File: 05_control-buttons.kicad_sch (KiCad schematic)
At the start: 8 parts, among them SW1 SW_Push, SW2 SW_Push, SW3 SW_Push, SW4 SW_Push

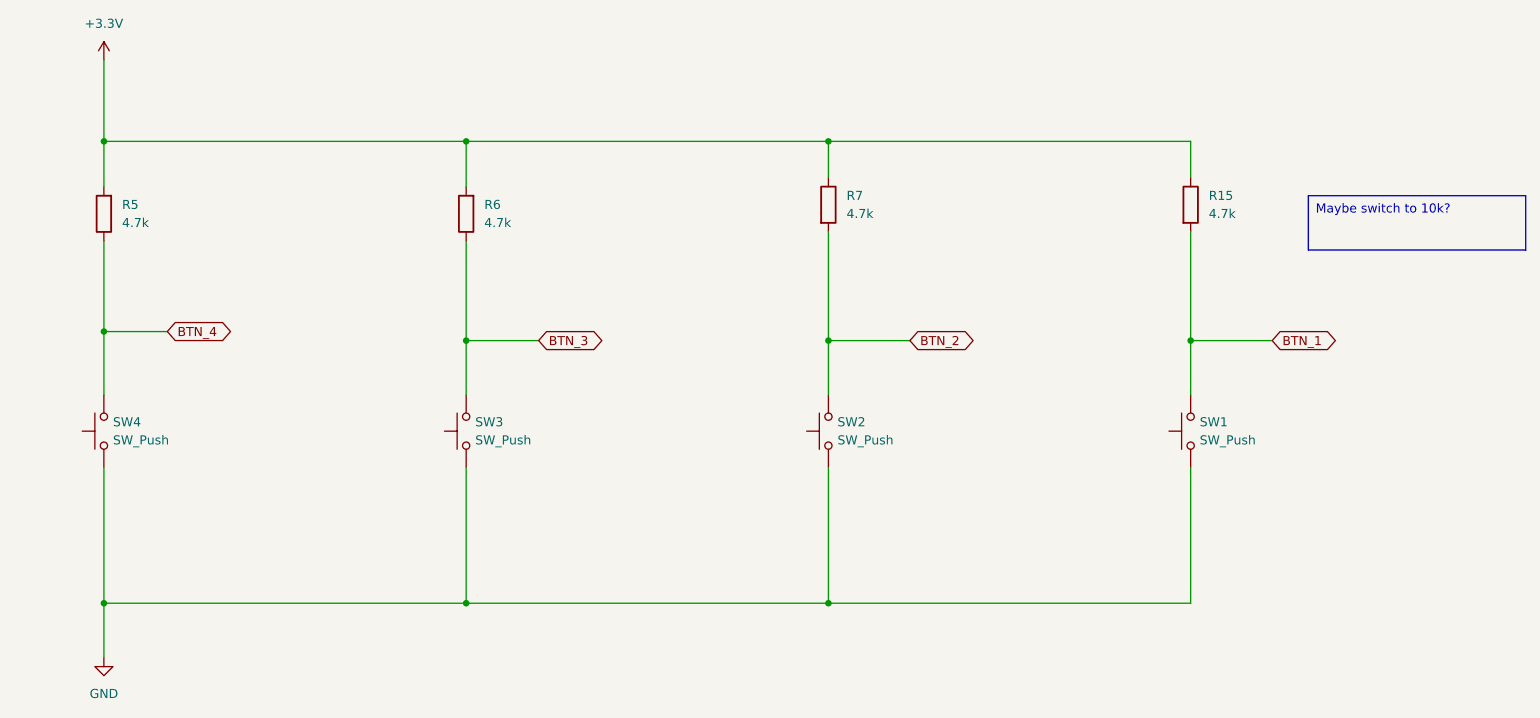
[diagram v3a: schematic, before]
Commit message: Migrate to KiCad 9, start working on the new revision
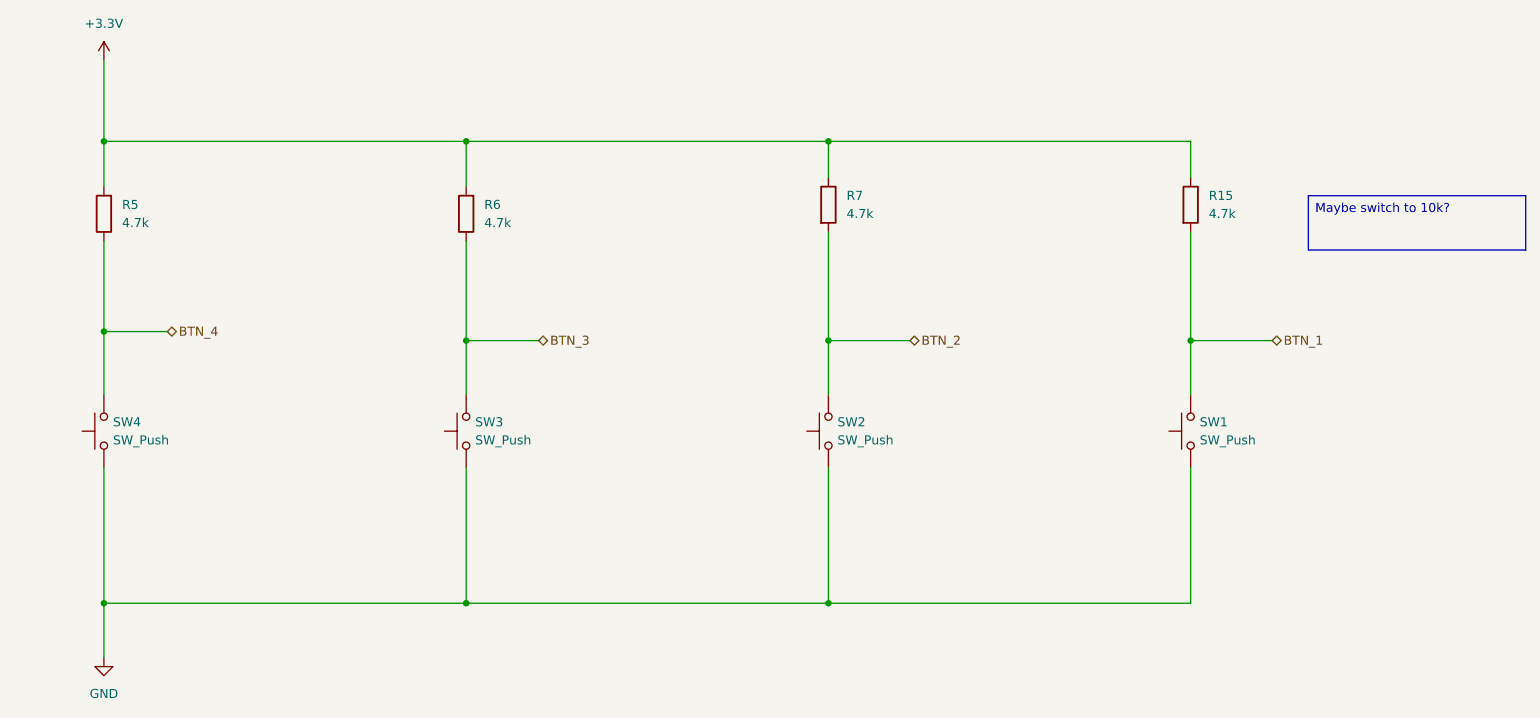
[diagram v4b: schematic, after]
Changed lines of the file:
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@@
 (kicad_sch
-	(version 20231120)
+	(version 20250114)
 	(generator "eeschema")
-	(generator_version "8.0")
+	(generator_version "9.0")
 	(paper "A4")
 	(title_block
@@
 		(comment 4 "Git revision: {kibot_git-hash}")
 	)
+	(text_box "Maybe switch to 10k?"
+		(exclude_from_sim no)
+		(at 241.3 66.04 0)
+		(size 30.48 7.62)
+		(margins 0.9525 0.9525 0.9525 0.9525)
+		(stroke
+			(width 0)
+			(type default)
+		)
+		(fill
+			(type none)
+		)
+		(effects
+			(font
+				(size 1.27 1.27)
+			)
+			(justify left top)
+		)
+	)
 	(junction
 		(at 173.99 123.19)
@@
 		)
 	)
-	(text_box "Maybe switch to 10k?"
-		(exclude_from_sim no)
-		(at 241.3 66.04 0)
-		(size 30.48 7.62)
-		(stroke
-			(width 0)
-			(type default)
-		)
-		(fill
-			(type none)
-		)
+	(hierarchical_label "BTN_3"
+		(shape bidirectional)
+		(at 133.35 86.36 0)
 		(effects
 			(font
 				(size 1.27 1.27)
 			)
-			(justify left top)
-		)
-	)
-	(global_label "BTN_3"
+			(justify left)
+		)
+	)
+	(hierarchical_label "BTN_4"
 		(shape bidirectional)
-		(at 133.35 86.36 0)
-		(fields_autoplaced yes)
+		(at 81.28 85.09 0)
 		(effects
 			(font
@@
 			(justify left)
 		)
-		(property "Intersheetrefs" "${INTERSHEET_REFS}"
-			(at 143.1917 86.36 0)
-			(effects
-				(font
-					(size 1.27 1.27)
-				)
-				(justify left)
-				(hide yes)
-			)
-		)
-	)
-	(global_label "BTN_1"
+	)
+	(hierarchical_label "BTN_2"
 		(shape bidirectional)
-		(at 236.22 86.36 0)
-		(fields_autoplaced yes)
+		(at 185.42 86.36 0)
 		(effects
 			(font
@@
 			(justify left)
 		)
-		(property "Intersheetrefs" "${INTERSHEET_REFS}"
-			(at 246.0617 86.36 0)
-			(effects
-				(font
-					(size 1.27 1.27)
-				)
-				(justify left)
-				(hide yes)
-			)
-		)
-	)
-	(global_label "BTN_4"
+	)
+	(hierarchical_label "BTN_1"
 		(shape bidirectional)
-		(at 81.28 85.09 0)
-		(fields_autoplaced yes)
+		(at 236.22 86.36 0)
 		(effects
 			(font
@@
 			)
 			(justify left)
-		)
-		(property "Intersheetrefs" "${INTERSHEET_REFS}"
-			(at 91.1217 85.09 0)
-			(effects
-				(font
-					(size 1.27 1.27)
-				)
-				(justify left)
-				(hide yes)
-			)
-		)
-	)
-	(global_label "BTN_2"
-		(shape bidirectional)
-		(at 185.42 86.36 0)
-		(fields_autoplaced yes)
-		(effects
-			(font
-				(size 1.27 1.27)
-			)
-			(justify left)
-		)
-		(property "Intersheetrefs" "${INTERSHEET_REFS}"
-			(at 195.2617 86.36 0)
-			(effects
-				(font
-					(size 1.27 1.27)
-				)
-				(justify left)
-				(hide yes)
-			)
 		)
 	)
@@
 			)
 		)
-		(property "Datasheet" "https://www.te.com/commerce/DocumentDelivery/DDEController?Action=srchrtrv&DocNm=1308111-1_SWITCHES_CORE_PROGRAM_CATALOG&DocType=Catalog%20Section&DocLang=English&DocFormat=pdf&PartCntxt=1825910-6"
+		(property "Datasheet" "~"
 			(at 118.11 99.06 0)
 			(effects
@@
 			)
 		)
-		(property "Datasheet" "https://www.te.com/commerce/DocumentDelivery/DDEController?Action=srchrtrv&DocNm=1308111-1_SWITCHES_CORE_PROGRAM_CATALOG&DocType=Catalog%20Section&DocLang=English&DocFormat=pdf&PartCntxt=1825910-6"
+		(property "Datasheet" "~"
 			(at 168.91 99.06 0)
 			(effects
@@
 			)
 		)
-		(property "Datasheet" "https://www.te.com/commerce/DocumentDelivery/DDEController?Action=srchrtrv&DocNm=1308111-1_SWITCHES_CORE_PROGRAM_CATALOG&DocType=Catalog%20Section&DocLang=English&DocFormat=pdf&PartCntxt=1825910-6"
+		(property "Datasheet" "~"
 			(at 219.71 99.06 0)
 			(effects
@@
 			)
 		)
-		(property "Datasheet" "https://www.te.com/commerce/DocumentDelivery/DDEController?Action=srchrtrv&DocNm=1308111-1_SWITCHES_CORE_PROGRAM_CATALOG&DocType=Catalog%20Section&DocLang=English&DocFormat=pdf&PartCntxt=1825910-6"
+		(property "Datasheet" "~"
 			(at 67.31 99.06 0)
 			(effects

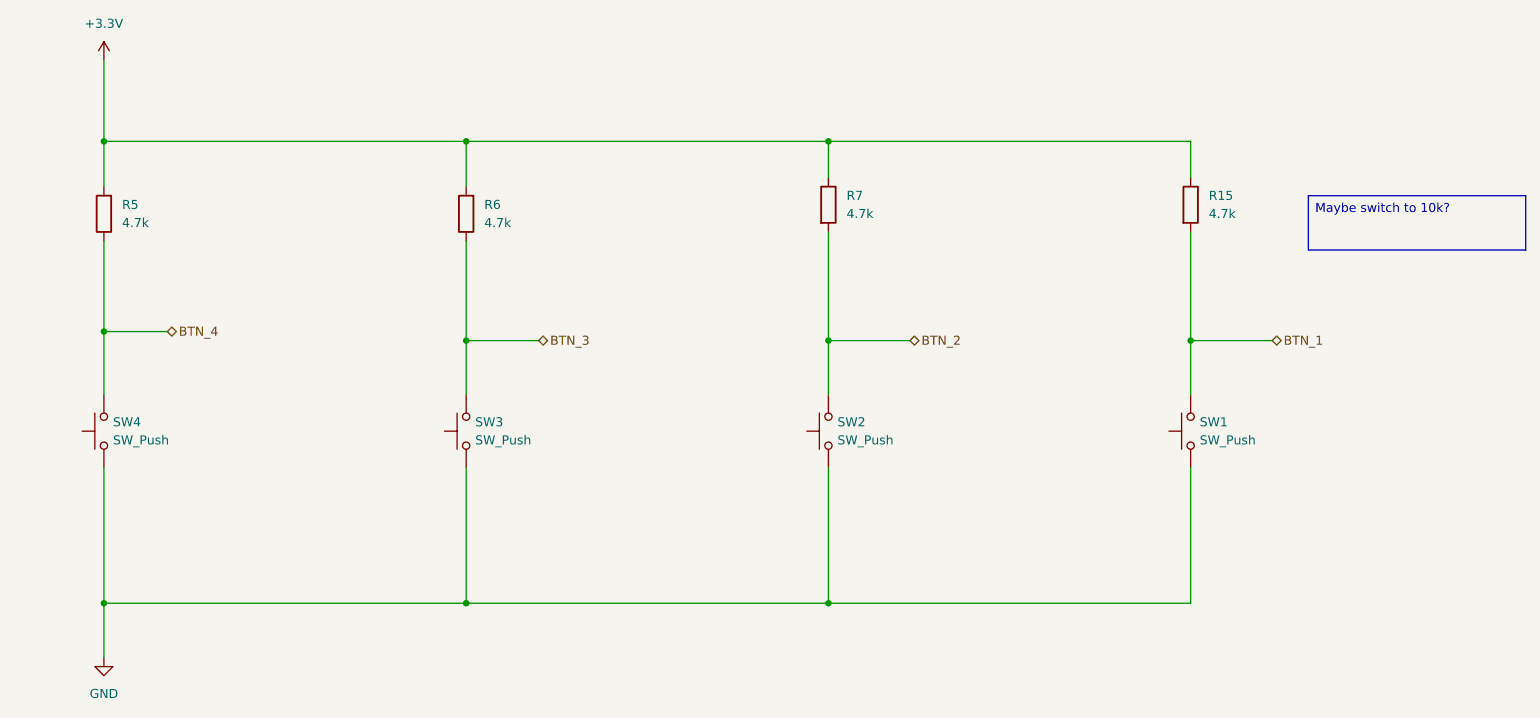
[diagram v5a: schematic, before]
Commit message: fully connect the sd connector, redraw sd and buttons
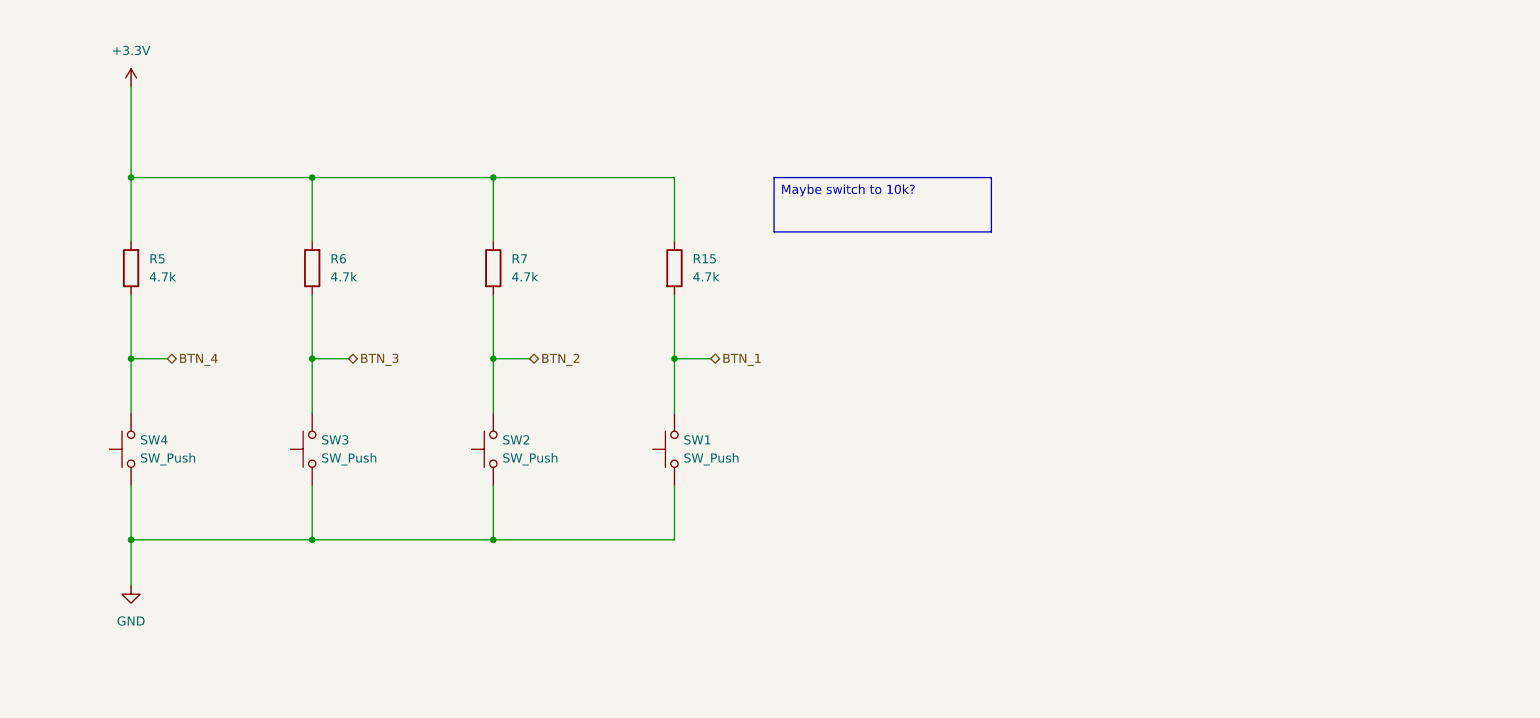
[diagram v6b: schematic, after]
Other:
- moved on the sheet: R15, R5, R6, R7, SW1, SW2, SW3, SW4

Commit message: v2: major changes
- Move to hierarchical labels
- use another RP Pico Footprint
- split power path in USB/charging and on/off with a button approach in order to control turning on and off
  with the RP Pico, make use of long presses and delay turning of the voltage in order to do a proper shutdown
- introduce another charging controller with a better performance an a lower voltage needed in order to charge the battery
- rework display booster circuit
- rework SD and buttons
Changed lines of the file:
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@@
 	)
 	(hierarchical_label "BTN_3"
-		(shape bidirectional)
+		(shape output)
 		(at 106.68 88.9 0)
 		(effects
@@
 	)
 	(hierarchical_label "BTN_4"
-		(shape bidirectional)
+		(shape output)
 		(at 81.28 88.9 0)
 		(effects
@@
 	)
 	(hierarchical_label "BTN_2"
-		(shape bidirectional)
+		(shape output)
 		(at 132.08 88.9 0)
 		(effects
@@
 	)
 	(hierarchical_label "BTN_1"
-		(shape bidirectional)
+		(shape output)
 		(at 157.48 88.9 0)
 		(effects

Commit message: v2: finished schematics, start routing
The schematics for v2 should be mostly finished by now.
The new on/off button is ready and tested with a breadboard setup.
It now uses two FETs for a self-holding circuit for turning the
device on and off. To reach a safe logic level for Pico 2, a
2.7V Zener diode is used together with a pull-down for E9 affected
RP2350 revisions.
Besides, most pull-up resistors are 10k now to keep the BoM
smaller.

Routing started with a major redesign.
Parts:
- R15, R5, R6, R7: value 4.7k -> 10k
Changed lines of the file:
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@@
 		(comment 4 "Git revision: {kibot_git-hash}")
-	)
-	(text_box "Maybe switch to 10k?"
-		(exclude_from_sim no)
-		(at 166.37 63.5 0)
-		(size 30.48 7.62)
-		(margins 0.9525 0.9525 0.9525 0.9525)
-		(stroke
-			(width 0)
-			(type default)
-		)
-		(fill
-			(type none)
-		)
-		(effects
-			(font
-				(size 1.27 1.27)
-			)
-			(justify left top)
-		)
 	)
 	(junction
@@
 			)
 		)
-		(property "Value" "4.7k"
+		(property "Value" "10k"
 			(at 104.14 77.4699 0)
 			(effects
@@
 			)
 		)
-		(property "Value" "4.7k"
+		(property "Value" "10k"
 			(at 154.94 77.4699 0)
 			(effects
@@
 			)
 		)
-		(property "Value" "4.7k"
+		(property "Value" "10k"
 			(at 78.74 77.4699 0)
 			(effects
@@
 			)
 		)
-		(property "Value" "4.7k"
+		(property "Value" "10k"
 			(at 129.54 77.4699 0)
 			(effects
